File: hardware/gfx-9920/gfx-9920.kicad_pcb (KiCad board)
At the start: 2 copper layers, 50 x 150 mm, 28 parts, among them J1 GFX_Connector_Input, J2 AV, J3 Sound L, J4 Sound R, U1 TMS9918, U2 74HCT04, U3 74HCT574, U4 74HCT574, U5 74HCT574, U6 HM62256ALP-10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

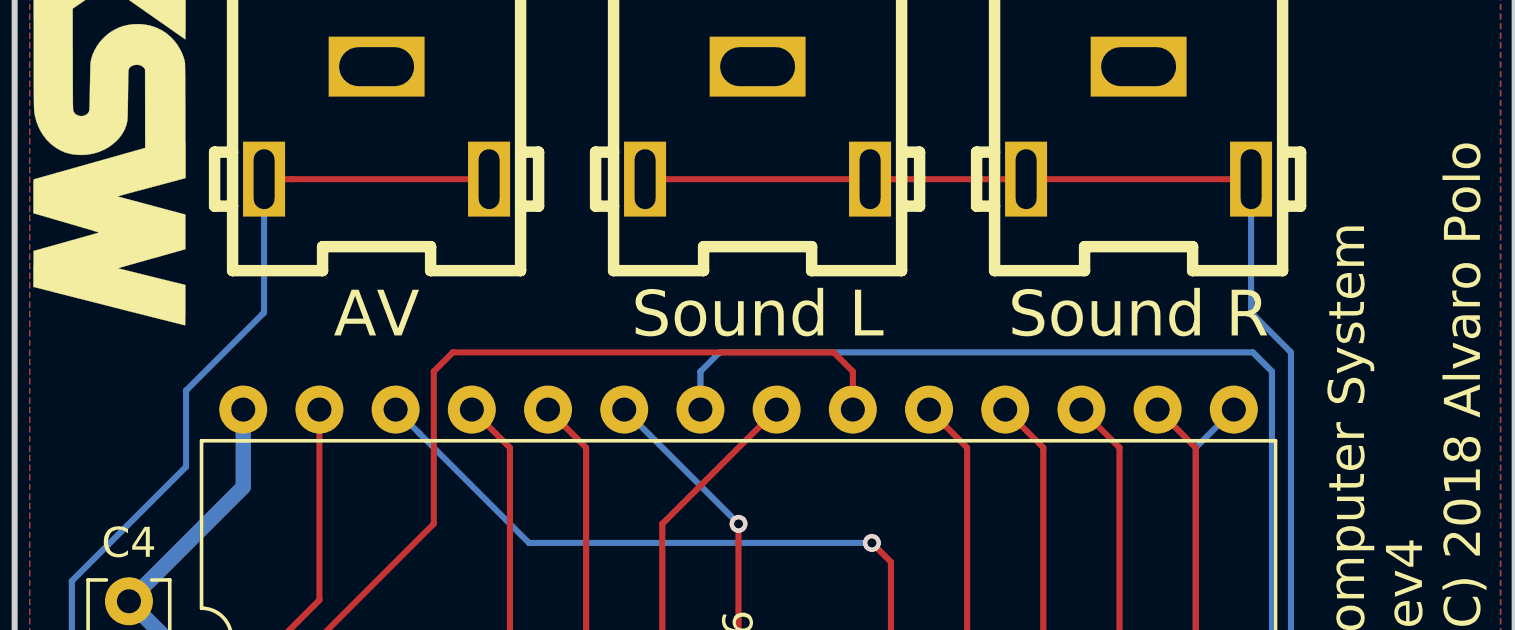
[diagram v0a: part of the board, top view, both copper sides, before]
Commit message: [GFX9920] Complete the first proposal of encoder circuit
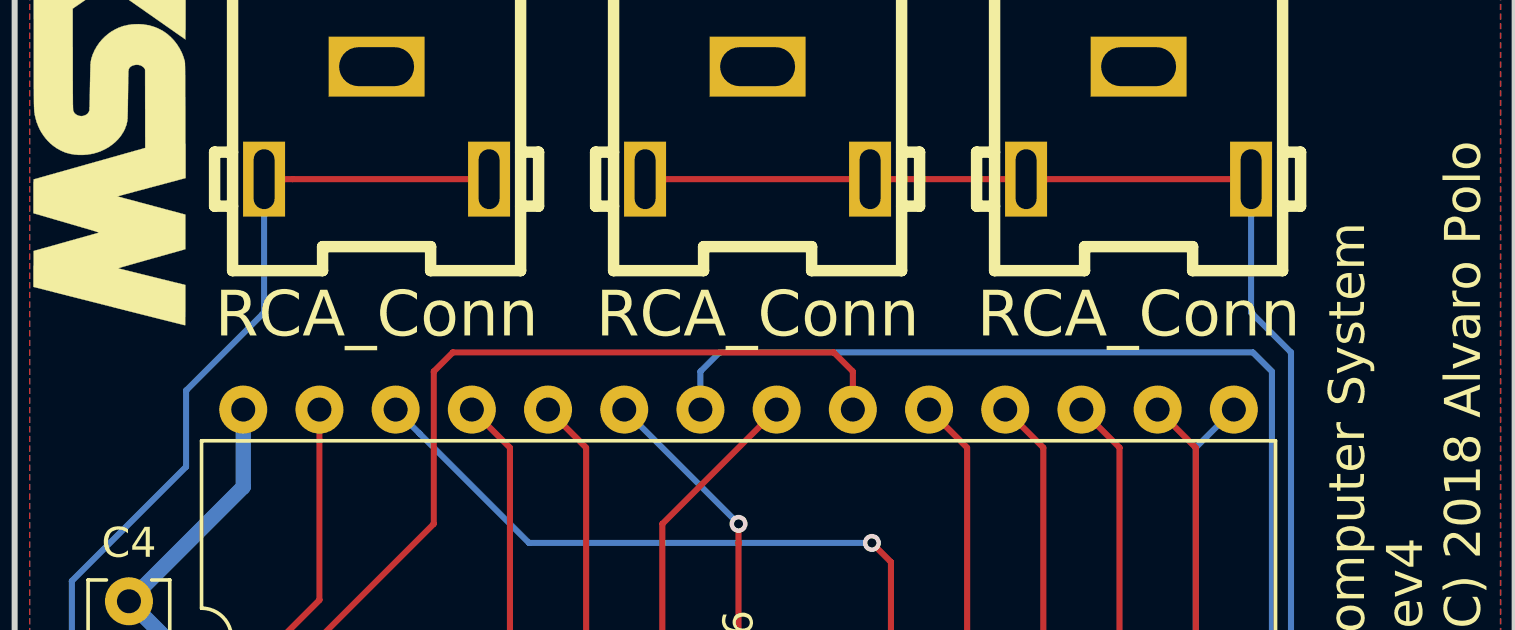
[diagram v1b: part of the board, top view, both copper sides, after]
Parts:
- J2: value AV -> RCA_Conn
- J3: value Sound L -> RCA_Conn
- J4: value Sound R -> RCA_Conn
- U6: value HM62256ALP-10 -> 62256
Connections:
- net /AD0 renamed /VRAM Decoding Logic/AD0
- net /AD1 renamed /VRAM Decoding Logic/AD1
- net /AD2 renamed /VRAM Decoding Logic/AD2
- net /AD3 renamed /VRAM Decoding Logic/AD3
- net /AD4 renamed /VRAM Decoding Logic/AD4
- net /AD5 renamed /VRAM Decoding Logic/AD5
- net /AD6 renamed /VRAM Decoding Logic/AD6
- net /AD7 renamed /VRAM Decoding Logic/AD7
- net /COL renamed Net-(U2-Pad12)
- net /DATA0 renamed /Input connector & power/DATA0
- net /DATA1 renamed /Input connector & power/DATA1
- net /DATA2 renamed /Input connector & power/DATA2
- net /DATA3 renamed /Input connector & power/DATA3
- net /DATA4 renamed /Input connector & power/DATA4
- net /DATA5 renamed /Input connector & power/DATA5
- net /DATA6 renamed /Input connector & power/DATA6
- net /DATA7 renamed /Input connector & power/DATA7
- net /MODE renamed /Input connector & power/A0
- net /RD renamed /VRAM Decoding Logic/RD
- net /ROW renamed Net-(U2-Pad6)
- net /SOUNDOUT renamed /Input connector & power/SOUNDOUT
- net /VD0 renamed /VRAM/RD0
- net /VD1 renamed /VRAM/RD1
- net /VD2 renamed /VRAM/RD2
- net /VD3 renamed /VRAM/RD3
- net /VD4 renamed /VRAM/RD4
- net /VD5 renamed /VRAM/RD5
- net /VD6 renamed /VRAM/RD6
- net /VD7 renamed /VRAM/RD7
- net /WR renamed /VRAM Decoding Logic/WR
- net /~CAS renamed /VRAM Decoding Logic/~CAS
- net /~CSR renamed /Input connector & power/BUSDIR
- net /~IRQ renamed /Input connector & power/~INT
- net /~RAS renamed /VRAM Decoding Logic/~RAS
- net /~RD renamed /Input connector & power/~RD
- net /~RESET renamed /Input connector & power/~RESET
- net /~VDPIOSL renamed /Input connector & power/~VDPIOSL
- net /~WR renamed /Input connector & power/~WR
- net Net-(J2-Pad1) renamed /Output connectors/CVBS
- net Net-(U1-Pad11) renamed /VRAM Decoding Logic/~WR
- net Net-(U1-Pad14) renamed /Interface Decoding Logic/~CSW
- net Net-(U4-Pad12) renamed /VRAM Decoding Logic/A6
- net Net-(U4-Pad13) renamed /VRAM Decoding Logic/A5
- net Net-(U4-Pad14) renamed /VRAM Decoding Logic/A4
- net Net-(U4-Pad15) renamed /VRAM Decoding Logic/A3
- net Net-(U4-Pad16) renamed /VRAM Decoding Logic/A2
- net Net-(U4-Pad17) renamed /VRAM Decoding Logic/A1
- net Net-(U4-Pad18) renamed /VRAM Decoding Logic/A0
- net Net-(U5-Pad12) renamed /VRAM Decoding Logic/A13
- net Net-(U5-Pad13) renamed /VRAM Decoding Logic/A12
- net Net-(U5-Pad14) renamed /VRAM Decoding Logic/A11
- net Net-(U5-Pad15) renamed /VRAM Decoding Logic/A10
- net Net-(U5-Pad16) renamed /VRAM Decoding Logic/A9
- net Net-(U5-Pad17) renamed /VRAM Decoding Logic/A8
- net Net-(U5-Pad18) renamed /VRAM Decoding Logic/A7
- U1 pad 35: GND -> Net-(U1-Pad35)
